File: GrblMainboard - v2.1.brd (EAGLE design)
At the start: 100 x 80 mm, 60 parts, among them IC1 LM7805

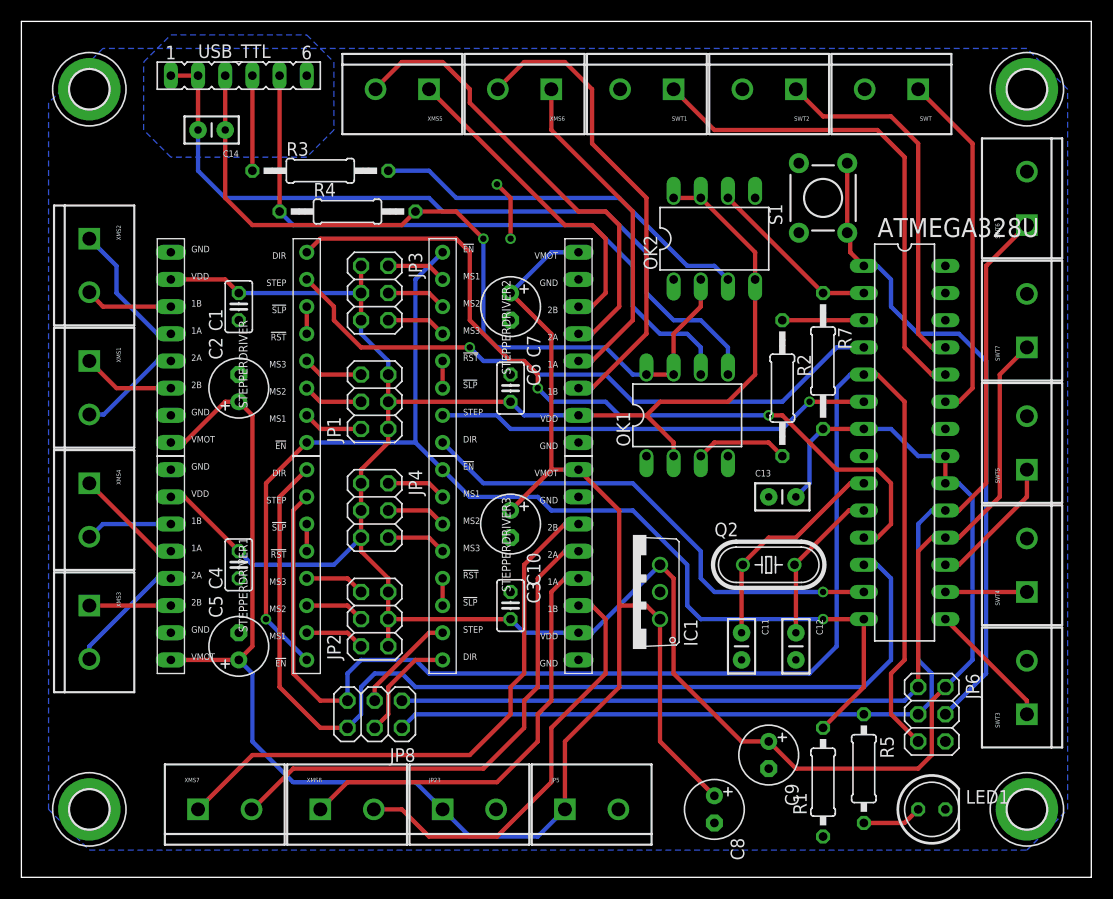
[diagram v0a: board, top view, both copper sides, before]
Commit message: Power wires thicker for ~ 3A
- make power wires thicker
- check for error in DRU schema and board
- replace Atmega328U with Atmega328
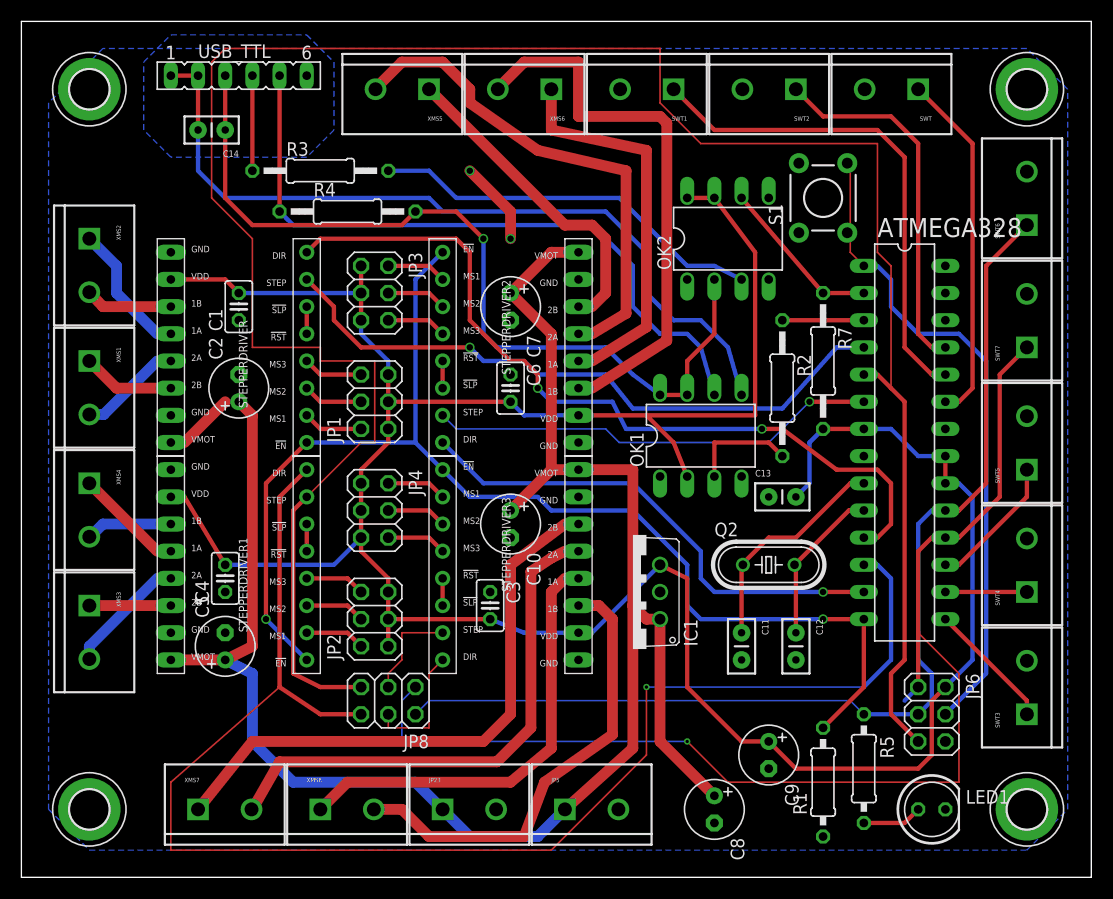
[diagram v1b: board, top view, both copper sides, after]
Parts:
- C10, C5, C7: value (none) -> 47uF
- JP1, JP2, JP3, JP4: value (none) -> microstep
- JP6: value (none) -> ICSP
- JP8: value (none) -> DualY
- LED1: value (none) -> Data
- Q2: value (none) -> 16 MHZ
- moved OK1 2.29 mm to (63.5, 41.3)
- moved C3 1.91 mm to (43.8, 25.4)
- moved C4 1.80 mm to (19.1, 27.9)
- moved JP8 1.80 mm to (34.3, 16.5)
- moved OK2 1.27 mm to (66.0, 59.7)
- moved C5 1.27 mm to (19.1, 21.6)
- renumbered ATMEGA328U to ATMEGA328
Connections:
- net !RESET1 renamed RESET
- net GND: now also H5.B3,6, H6.B3,6, H7.B3,6, H8.B3,6
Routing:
- net Y-STEP: track 138.9 -> 211.7 mm
- net Y-DIR: track 96.0 -> 138.7 mm, vias 0 -> 1
- net SPINDLE-ENABLE: track 86.2 -> 114.0 mm, vias 0 -> 1
- net N$20: track 44.4 -> 52.1 mm
- net N$19: track 31.4 -> 36.7 mm
- net 5V: track 259.7 -> 264.4 mm
- net USB_5V: track 76.4 -> 80.2 mm
- net 12V: track 173.9 -> 177.7 mm
- net N$18: track 43.4 -> 46.8 mm
- net N$28: track 40.2 -> 42.8 mm
- net GND: track 5.61 -> 7.93 mm
- net USB_AIFO: track 62.1 -> 64.2 mm
- net GNDA: track 72.6 -> 74.7 mm
- net N$26: track 48.0 -> 49.6 mm
- net A-DIR: track 10.5 -> 12.0 mm
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
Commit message: Add pullup Resistor for Atmel Reset pin
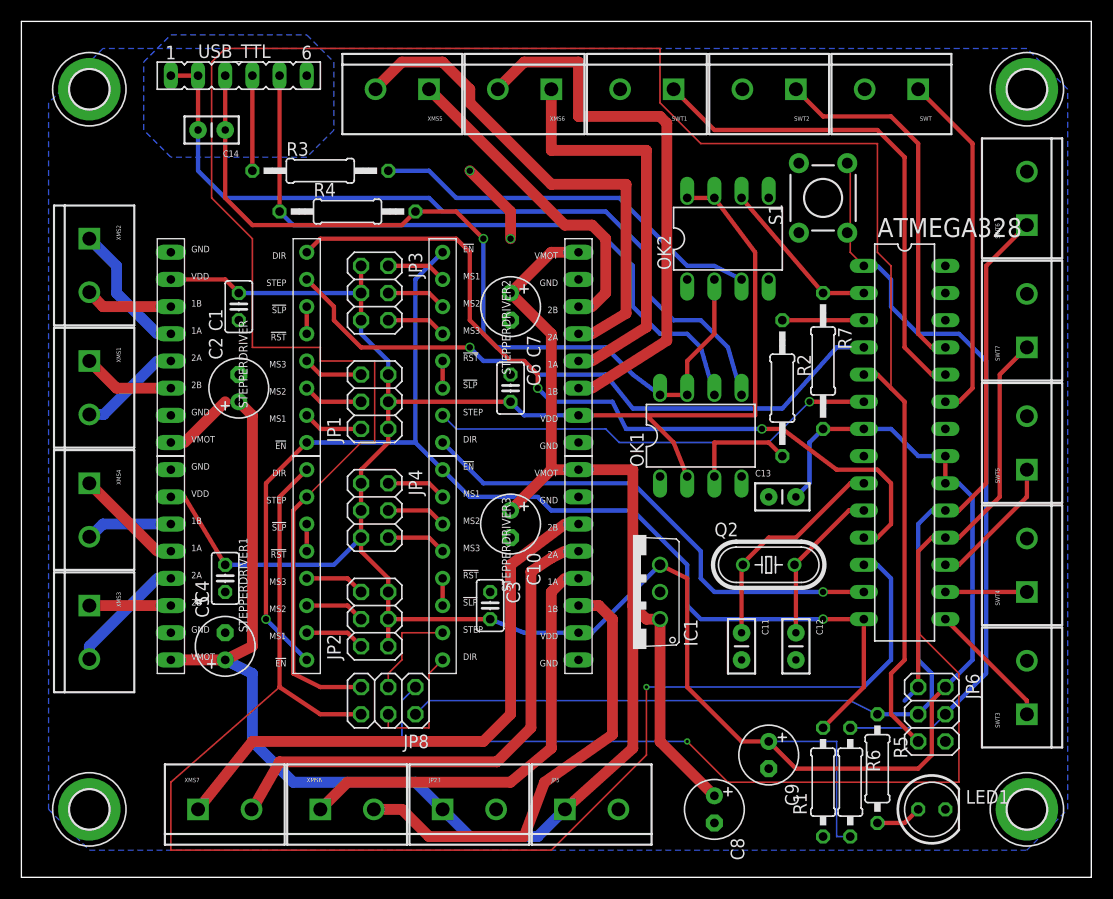
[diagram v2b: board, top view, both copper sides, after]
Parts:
- added R6: 10k, resistor:0207/10
- moved R5 1.27 mm to (80.0, 10.2)
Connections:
- net 5V: now also R6.2
- net RESET: now also R6.1
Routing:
- net 5V: track 264.4 -> 280.9 mm
- net RESET: track 61.5 -> 70.9 mm
- net N$19: track 36.7 -> 38.4 mm
- net N$37: track 5.61 -> 4.34 mm
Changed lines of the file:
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@@
 <element name="JP5" library="SparkFun" package="SCREWTERMINAL-5MM-2" value="FAN_MOTOR" x="50.8" y="6.35"/>
 <element name="JP6" library="pinhead" package="2X03" value="ICSP" x="85.09" y="15.24" rot="R270"/>
-<element name="R5" library="resistor" package="0207/10" value="1k" x="78.74" y="10.16" rot="R270"/>
+<element name="R5" library="resistor" package="0207/10" value="1k" x="80.01" y="10.16" rot="R270"/>
 <element name="LED1" library="led" package="LED5MM" value="Data" x="85.09" y="6.35"/>
 <element name="S1" library="SparkFun" package="TACTILE-PTH" value="RESET" x="74.93" y="63.5" rot="R90"/>
@@
 <element name="SWT6" library="SparkFun" package="SCREWTERMINAL-5MM-2" value="SPINDLE-DIR" x="93.98" y="60.96" rot="R90"/>
 <element name="SWT7" library="SparkFun" package="SCREWTERMINAL-5MM-2" value="SPINDLE-ENABLE" x="93.98" y="49.53" rot="R90"/>
+<element name="R6" library="resistor" package="0207/10" value="10k" x="77.47" y="8.89" rot="R270"/>
 </elements>
 <signals>
@@
 <wire x1="60.96" y1="40.64" x2="58.42" y2="43.18" width="0.4064" layer="1"/>
 <wire x1="68.58" y1="58.42" x2="64.77" y2="63.5" width="0.4064" layer="1"/>
+<contactref element="R6" pad="2"/>
+<wire x1="76.2" y1="12.7" x2="76.2" y2="3.81" width="0.1524" layer="16"/>
+<wire x1="69.85" y1="12.7" x2="76.2" y2="12.7" width="0.1524" layer="16"/>
+<wire x1="76.2" y1="3.81" x2="77.47" y2="3.81" width="0.1524" layer="16"/>
 </signal>
 <signal name="AIFO">
@@
 <wire x1="39.37" y1="76.2" x2="41.91" y2="73.66" width="1.016" layer="1"/>
 <wire x1="41.91" y1="73.66" x2="41.91" y2="72.39" width="1.016" layer="1"/>
-<wire x1="41.91" y1="72.39" x2="48.26" y2="67.945" width="1.016" layer="1"/>
-<wire x1="48.26" y1="67.945" x2="56.515" y2="66.04" width="1.016" layer="1"/>
-<wire x1="56.515" y1="66.04" x2="56.515" y2="52.705" width="1.016" layer="1"/>
+<wire x1="41.91" y1="72.39" x2="49.53" y2="64.77" width="1.016" layer="1"/>
+<wire x1="49.53" y1="64.77" x2="56.515" y2="64.77" width="1.016" layer="1"/>
+<wire x1="56.515" y1="64.77" x2="56.515" y2="52.705" width="1.016" layer="1"/>
 <wire x1="56.515" y1="52.705" x2="53.34" y2="50.8" width="1.016" layer="1"/>
 <wire x1="53.34" y1="50.8" x2="52.07" y2="50.8" width="0.4064" layer="1"/>
@@
 <contactref element="STEPPERDRIVER2" pad="1A"/>
 <contactref element="XMS6" pad="1"/>
-<wire x1="49.53" y1="73.66" x2="49.53" y2="69.85" width="1.016" layer="1"/>
-<wire x1="49.53" y1="69.85" x2="58.42" y2="67.945" width="1.016" layer="1"/>
+<wire x1="49.53" y1="73.66" x2="49.53" y2="67.945" width="1.016" layer="1"/>
+<wire x1="49.53" y1="67.945" x2="58.42" y2="67.945" width="1.016" layer="1"/>
 <wire x1="53.34" y1="48.26" x2="52.07" y2="48.26" width="0.4064" layer="1"/>
 <wire x1="58.42" y1="67.945" x2="58.42" y2="51.435" width="1.016" layer="1"/>
@@
 <wire x1="87.63" y1="34.29" x2="86.36" y2="34.29" width="0.4064" layer="1"/>
 <wire x1="85.09" y1="34.29" x2="86.36" y2="34.29" width="0.4064" layer="16"/>
-<wire x1="78.74" y1="15.24" x2="83.82" y2="15.24" width="0.4064" layer="16"/>
+<wire x1="80.01" y1="15.24" x2="83.82" y2="15.24" width="0.4064" layer="16"/>
 <wire x1="85.09" y1="34.29" x2="83.82" y2="33.02" width="0.4064" layer="16"/>
 <wire x1="83.82" y1="33.02" x2="83.82" y2="20.32" width="0.4064" layer="16"/>
@@
 <wire x1="38.1" y1="16.51" x2="36.83" y2="15.24" width="0.1524" layer="16"/>
 <wire x1="77.47" y1="16.51" x2="38.1" y2="16.51" width="0.1524" layer="16"/>
-<wire x1="78.74" y1="15.24" x2="77.47" y2="16.51" width="0.1524" layer="16"/>
+<wire x1="80.01" y1="15.24" x2="77.47" y2="16.51" width="0.1524" layer="16"/>
 </signal>
 <signal name="A-STEP">
@@
 <contactref element="R5" pad="2"/>
 <contactref element="LED1" pad="A"/>
-<wire x1="78.74" y1="5.08" x2="82.55" y2="5.08" width="0.4064" layer="1"/>
+<wire x1="80.01" y1="5.08" x2="82.55" y2="5.08" width="0.4064" layer="1"/>
 <wire x1="82.55" y1="5.08" x2="83.82" y2="6.35" width="0.4064" layer="1"/>
 </signal>
@@
 <wire x1="77.47" y1="60.96" x2="77.1906" y2="60.2488" width="0.1524" layer="1"/>
 <wire x1="80.01" y1="57.15" x2="78.74" y2="57.15" width="0.1524" layer="16"/>
+<contactref element="R6" pad="1"/>
+<wire x1="85.09" y1="13.97" x2="77.47" y2="13.97" width="0.1524" layer="16"/>
+<wire x1="86.36" y1="15.24" x2="85.09" y2="13.97" width="0.1524" layer="16"/>
 </signal>
 <signal name="G-RESET">
